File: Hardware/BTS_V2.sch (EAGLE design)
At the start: 66 parts, among them IC1 TPA3140D2PWP, IC2 BLK-MD-SPK-B, J1 SPKR_OUT, J2 RN52BoB_R, J3 RN52BoB_L, J4 TFT_CONNECTION, J6 HC-05, T3_2 TEENSY_3.1-3.2_DIL

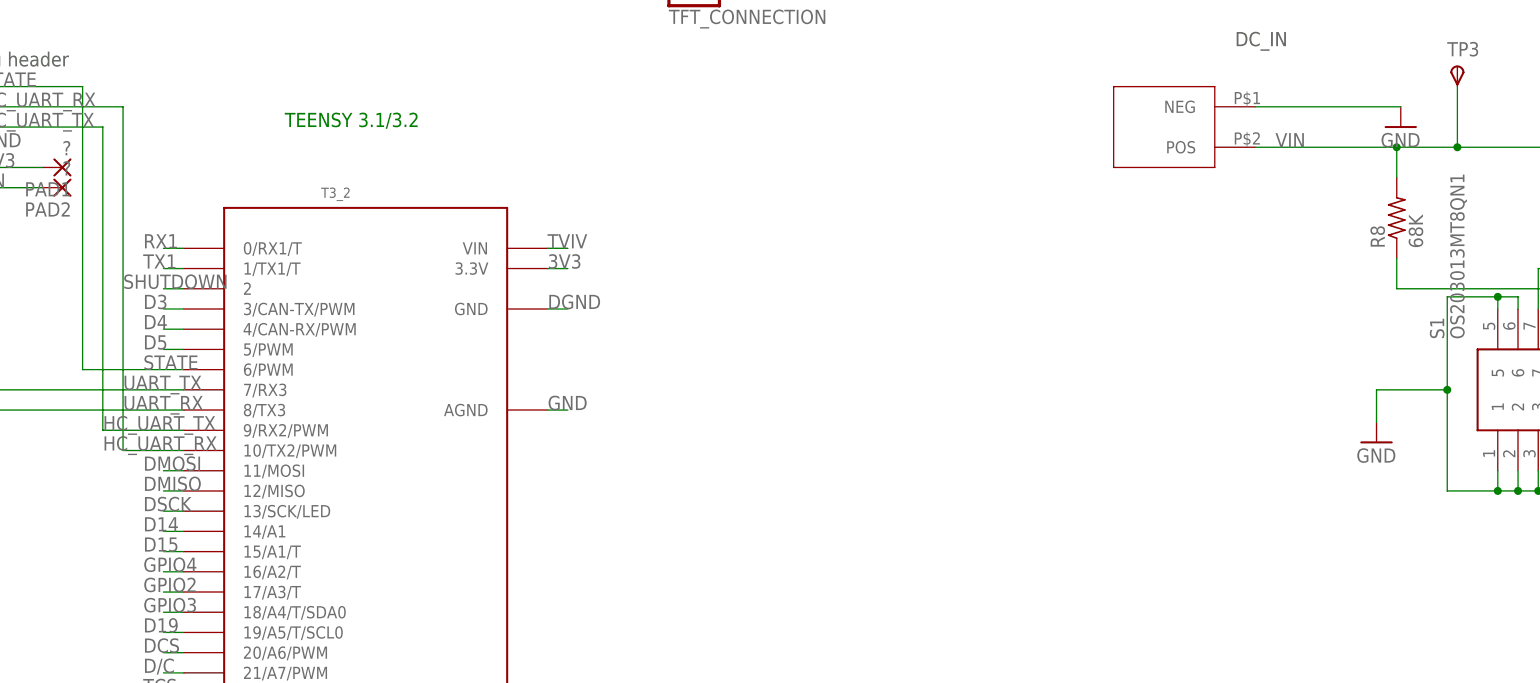
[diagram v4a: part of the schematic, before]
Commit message: Finally solved the issue - was a too large cap on output
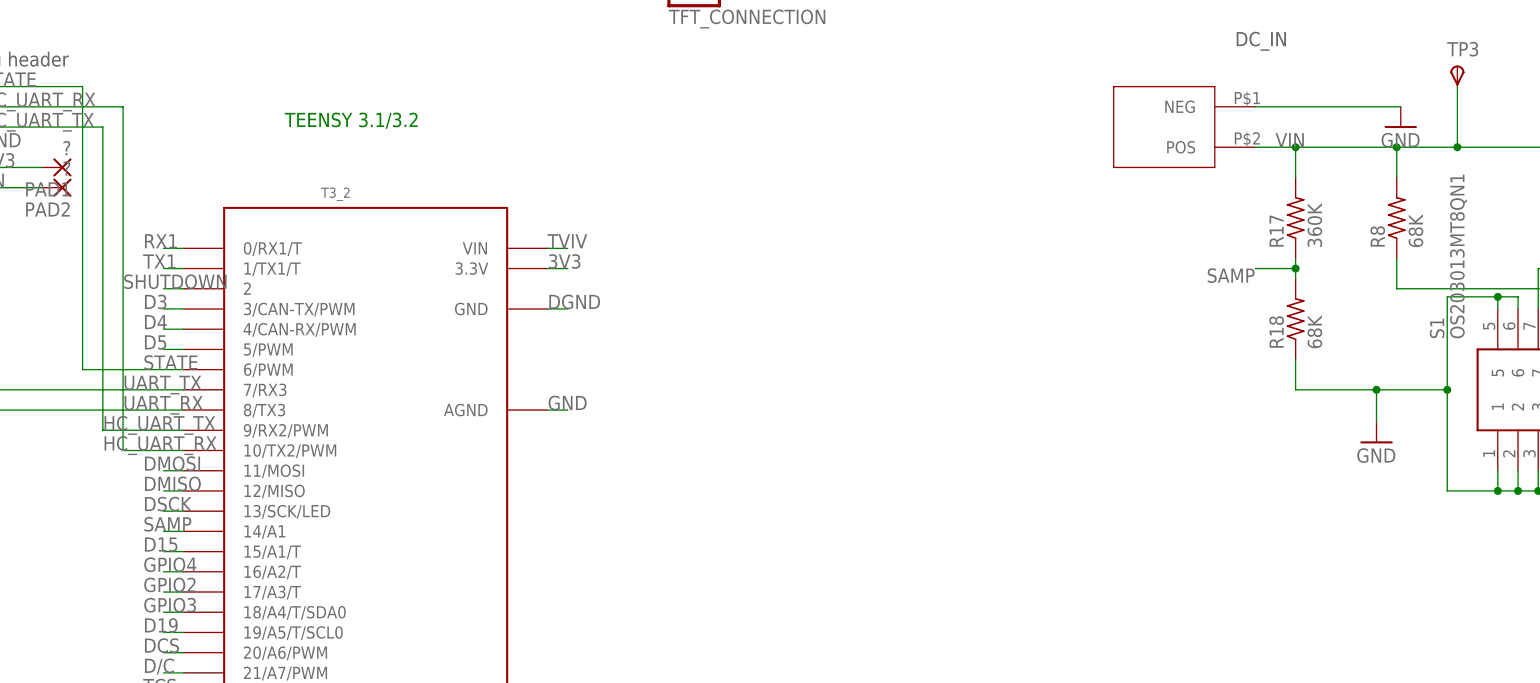
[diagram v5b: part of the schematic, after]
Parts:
- added R17: 360K, resistor:R-US_R0603
- added R18: 68K, resistor:R-US_R0603
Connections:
- removed net D14: T3_2.14/A1
- new net SAMP: R17.1, R18.2, T3_2.14/A1
- net GND: now also R18.1
- net VIN: now also R17.2
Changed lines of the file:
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@@
 <part name="TP7" library="testpad" library_urn="urn:adsk.eagle:library:385" deviceset="TPS" device="PAD1-17" package3d_urn="urn:adsk.eagle:package:27949/1"/>
 <part name="TP8" library="testpad" library_urn="urn:adsk.eagle:library:385" deviceset="TPS" device="PAD1-17" package3d_urn="urn:adsk.eagle:package:27949/1"/>
+<part name="R17" library="resistor" library_urn="urn:adsk.eagle:library:348" deviceset="R-US_" device="R0603" package3d_urn="urn:adsk.eagle:package:26057/1" value="360K">
+<attribute name="RESISTANCE" value="68K"/>
+</part>
+<part name="R18" library="resistor" library_urn="urn:adsk.eagle:library:348" deviceset="R-US_" device="R0603" package3d_urn="urn:adsk.eagle:package:26057/1" value="68K">
+<attribute name="RESISTANCE" value="68K"/>
+</part>
 </parts>
 <sheets>
@@
 <instance part="TP7" gate="G$1" x="229.362" y="45.72" rot="R180"/>
 <instance part="TP8" gate="G$1" x="220.98" y="45.72" rot="R180"/>
+<instance part="R17" gate="G$1" x="218.44" y="181.61" rot="R90"/>
+<instance part="R18" gate="G$1" x="218.44" y="168.91" rot="R90"/>
 </instances>
 <busses>
@@
 <wire x1="228.6" y1="160.02" x2="237.49" y2="160.02" width="0.1524" layer="91"/>
 <junction x="237.49" y="160.02"/>
+<pinref part="R18" gate="G$1" pin="1"/>
+<wire x1="228.6" y1="160.02" x2="218.44" y2="160.02" width="0.1524" layer="91"/>
+<wire x1="218.44" y1="160.02" x2="218.44" y2="163.83" width="0.1524" layer="91"/>
+<junction x="228.6" y="160.02"/>
 </segment>
 <segment>
@@
 <wire x1="261.62" y1="187.96" x2="261.62" y2="190.5" width="0.1524" layer="91"/>
 <label x="215.9" y="190.5" size="1.778" layer="95"/>
-<wire x1="213.36" y1="190.5" x2="231.14" y2="190.5" width="0.1524" layer="91"/>
+<wire x1="213.36" y1="190.5" x2="218.44" y2="190.5" width="0.1524" layer="91"/>
+<wire x1="218.44" y1="190.5" x2="231.14" y2="190.5" width="0.1524" layer="91"/>
 <wire x1="231.14" y1="190.5" x2="238.76" y2="190.5" width="0.1524" layer="91"/>
 <wire x1="238.76" y1="190.5" x2="261.62" y2="190.5" width="0.1524" layer="91"/>
@@
 <wire x1="238.76" y1="198.12" x2="238.76" y2="190.5" width="0.1524" layer="91"/>
 <junction x="238.76" y="190.5"/>
+<wire x1="218.44" y1="186.69" x2="218.44" y2="190.5" width="0.1524" layer="91"/>
+<junction x="218.44" y="190.5"/>
+<pinref part="R17" gate="G$1" pin="2"/>
 </segment>
 </net>
@@
 </segment>
 </net>
-<net name="D14" class="0">
-<segment>
-<pinref part="T3_2" gate="G$1" pin="14/A1"/>
-<wire x1="78.74" y1="142.24" x2="76.2" y2="142.24" width="0.1524" layer="91"/>
-<label x="73.66" y="142.24" size="1.778" layer="95"/>
-</segment>
-</net>
 <net name="D15" class="0">
 <segment>
@@
 </segment>
 </net>
+<net name="SAMP" class="0">
+<segment>
+<pinref part="R18" gate="G$1" pin="2"/>
+<pinref part="R17" gate="G$1" pin="1"/>
+<wire x1="218.44" y1="176.53" x2="218.44" y2="175.26" width="0.1524" layer="91"/>
+<label x="213.36" y="175.26" size="1.778" layer="95" rot="R180"/>
+<wire x1="218.44" y1="175.26" x2="218.44" y2="173.99" width="0.1524" layer="91"/>
+<wire x1="218.44" y1="175.26" x2="213.36" y2="175.26" width="0.1524" layer="91"/>
+<junction x="218.44" y="175.26"/>
+</segment>
+<segment>
+<pinref part="T3_2" gate="G$1" pin="14/A1"/>
+<wire x1="78.74" y1="142.24" x2="76.2" y2="142.24" width="0.1524" layer="91"/>
+<label x="73.66" y="142.24" size="1.778" layer="95"/>
+</segment>
+</net>

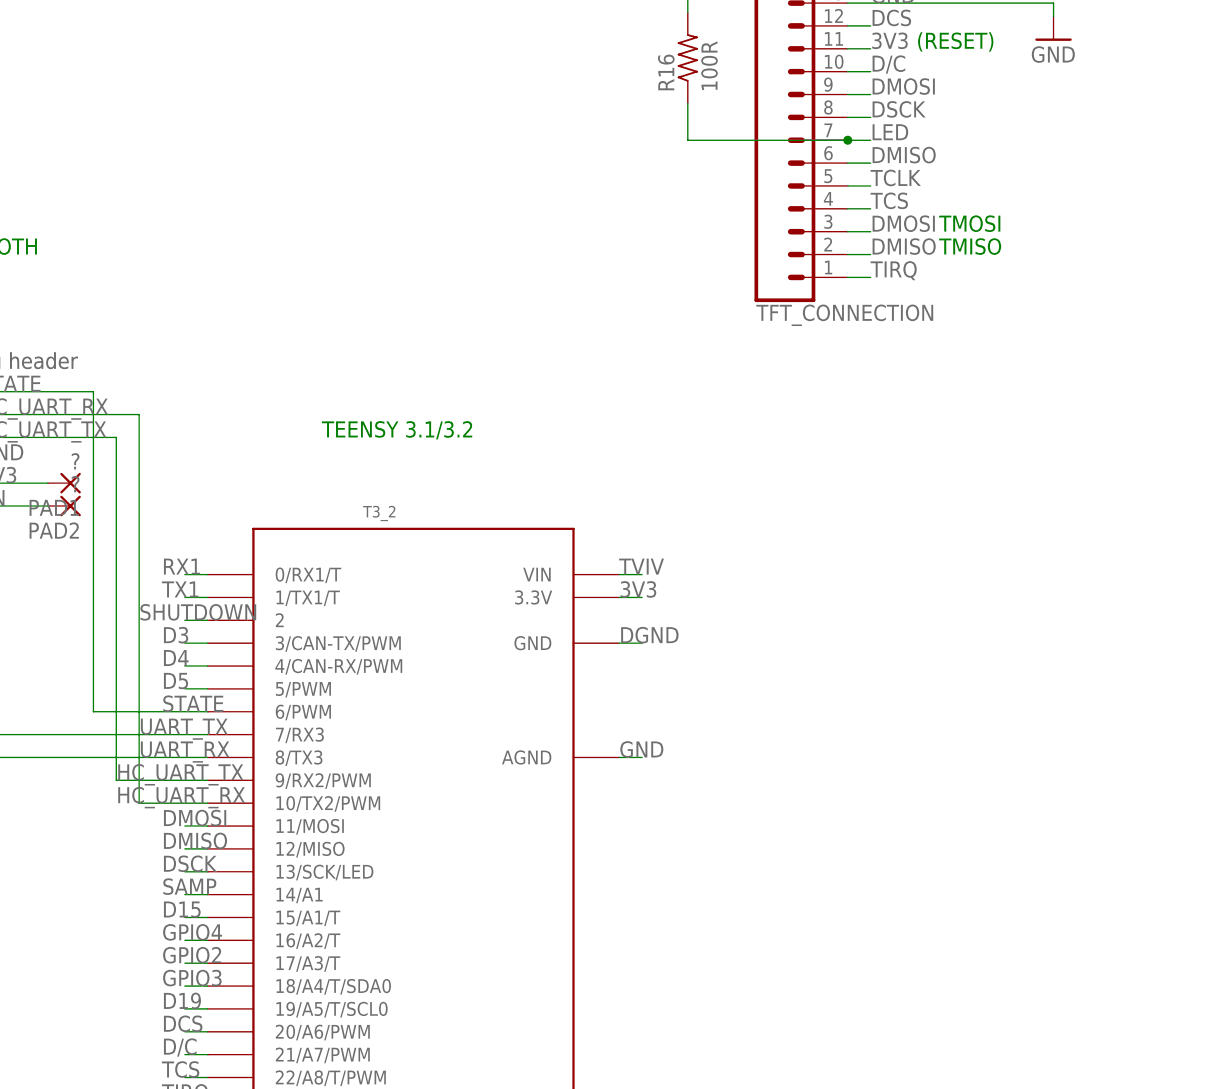
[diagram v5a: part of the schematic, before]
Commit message: Fixed two HW issues
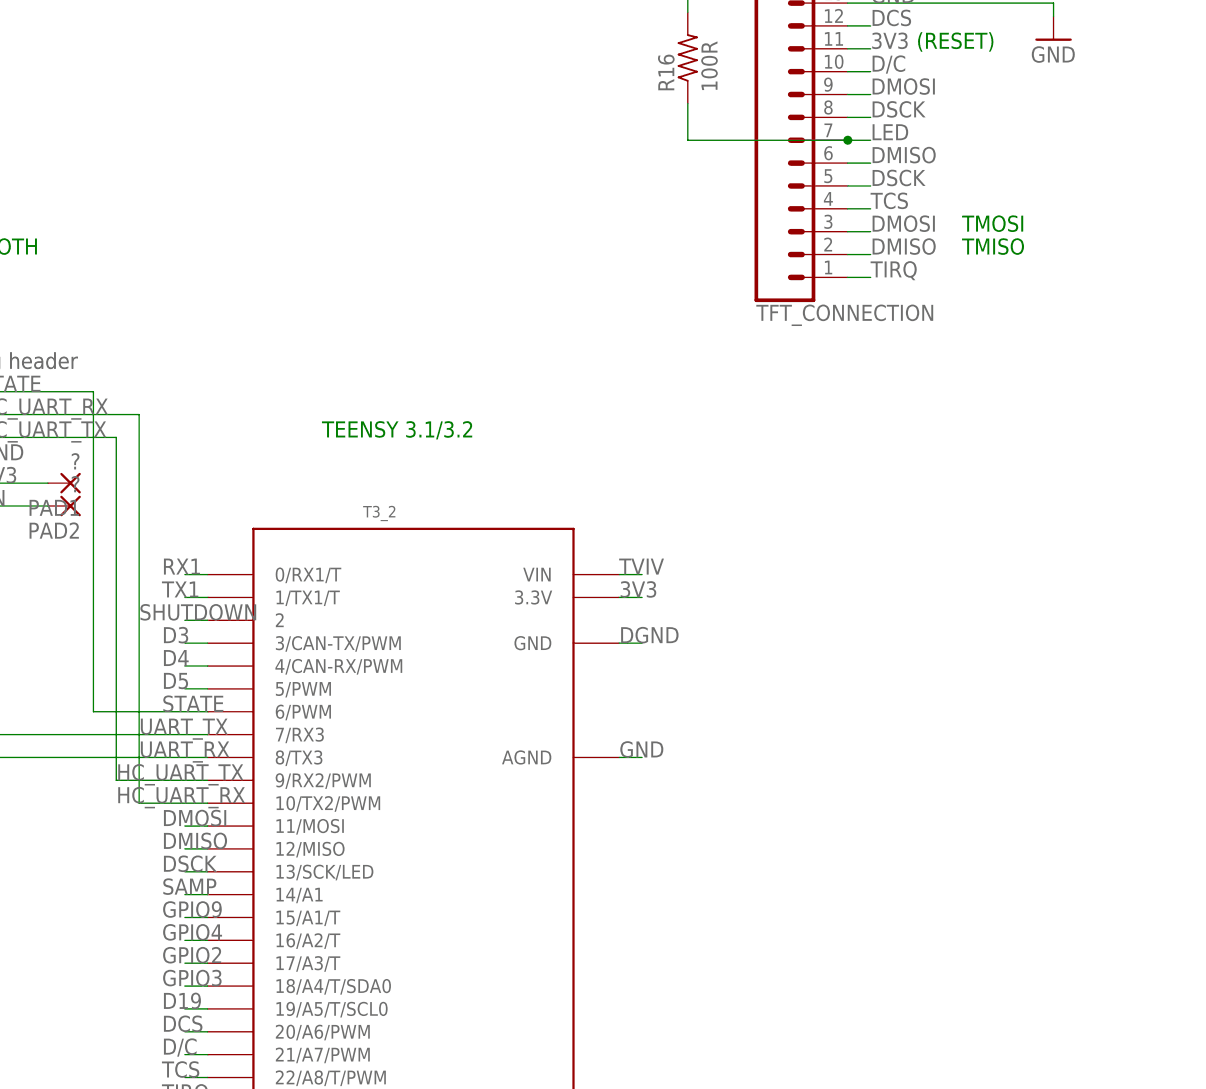
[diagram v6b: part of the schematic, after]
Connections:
- removed net D15: T3_2.15/A1/T
- removed net TCLK: J4.5
- net DSCK: now also J4.5
- net GPIO9: now also T3_2.15/A1/T
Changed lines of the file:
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@@
 <?xml version="1.0" encoding="utf-8"?>
 <!DOCTYPE eagle SYSTEM "eagle.dtd">
-<eagle version="8.7.0">
+<eagle version="9.0.1">
 <drawing>
 <settings>
-<setting alwaysvectorfont="yes"/>
+<setting alwaysvectorfont="no"/>
 <setting verticaltext="up"/>
 </settings>
@@
 <text x="378.46" y="7.62" size="2.54" layer="97">v1.0</text>
 <text x="157.48" y="236.22" size="1.778" layer="91">(RESET)</text>
-<text x="160.02" y="215.9" size="1.778" layer="91">TMOSI</text>
-<text x="160.02" y="213.36" size="1.778" layer="91">TMISO</text>
+<text x="162.56" y="215.9" size="1.778" layer="91">TMOSI</text>
+<text x="162.56" y="213.36" size="1.778" layer="91">TMISO</text>
 <text x="45.72" y="104.14" size="1.778" layer="91">Maybe try to remove the LDO and power the BT module from the 3v3 layout - I dont know if this works as of yet.</text>
 <text x="142.24" y="254" size="1.778" layer="91">TFT</text>
@@
 <label x="38.1" y="63.5" size="1.778" layer="95"/>
 </segment>
+<segment>
+<pinref part="T3_2" gate="G$1" pin="15/A1/T"/>
+<wire x1="78.74" y1="139.7" x2="76.2" y2="139.7" width="0.1524" layer="91"/>
+<label x="73.66" y="139.7" size="1.778" layer="95"/>
+</segment>
 </net>
 <net name="GPIO10" class="0">
@@
 </segment>
 </net>
-<net name="D15" class="0">
-<segment>
-<pinref part="T3_2" gate="G$1" pin="15/A1/T"/>
-<wire x1="78.74" y1="139.7" x2="76.2" y2="139.7" width="0.1524" layer="91"/>
-<label x="73.66" y="139.7" size="1.778" layer="95"/>
-</segment>
-</net>
 <net name="D19" class="0">
 <segment>
@@
 <wire x1="76.2" y1="144.78" x2="78.74" y2="144.78" width="0.1524" layer="91"/>
 <label x="73.66" y="144.78" size="1.778" layer="95"/>
+</segment>
+<segment>
+<pinref part="J4" gate="G$1" pin="5"/>
+<wire x1="149.86" y1="220.98" x2="152.4" y2="220.98" width="0.1524" layer="91"/>
+<label x="152.4" y="220.98" size="1.778" layer="95"/>
 </segment>
 </net>
@@
 </segment>
 </net>
-<net name="TCLK" class="0">
-<segment>
-<pinref part="J4" gate="G$1" pin="5"/>
-<wire x1="149.86" y1="220.98" x2="152.4" y2="220.98" width="0.1524" layer="91"/>
-<label x="152.4" y="220.98" size="1.778" layer="95"/>
-</segment>
-</net>
